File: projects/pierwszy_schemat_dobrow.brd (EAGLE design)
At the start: 100 x 80 mm, 36 parts, among them IC1 74HC595N, IC2 7805T, IC3 LD117AV

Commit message: Done power section
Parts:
- moved IC2 178.9 mm to (90.1, 63.9), flipped to the bottom, turned to 90 degrees
- moved C2 142.0 mm to (85.2, 74.5), turned to 90 degrees
- moved IC3 123.7 mm to (70.0, 64.0), turned to 90 degrees
- moved C1 119.9 mm to (74.4, 74.3), turned to 90 degrees
- moved U$1 14.3 mm to (51.0, 38.9)
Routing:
- net GND: track 0.00 -> 34.0 mm, vias 0 -> 1
- net VCC_5V: track 0.00 -> 13.8 mm
- net VIN_9V: track 0.00 -> 12.8 mm, vias 0 -> 1

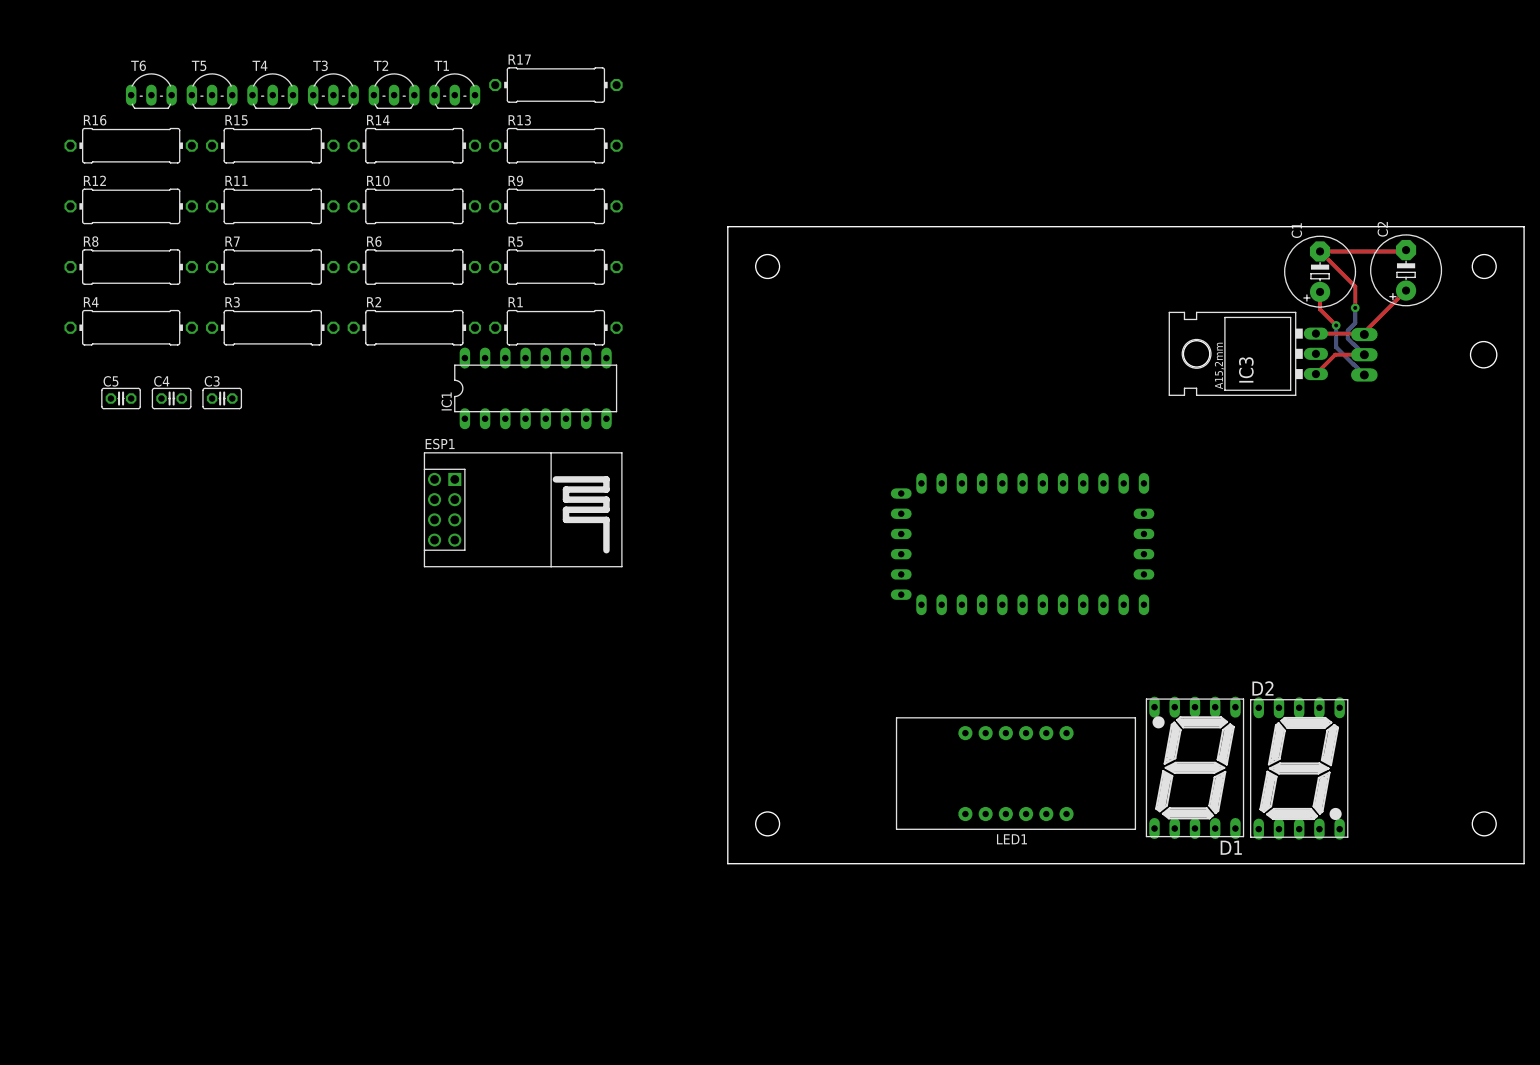
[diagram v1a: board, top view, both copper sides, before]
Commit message: Added ESP-01 module
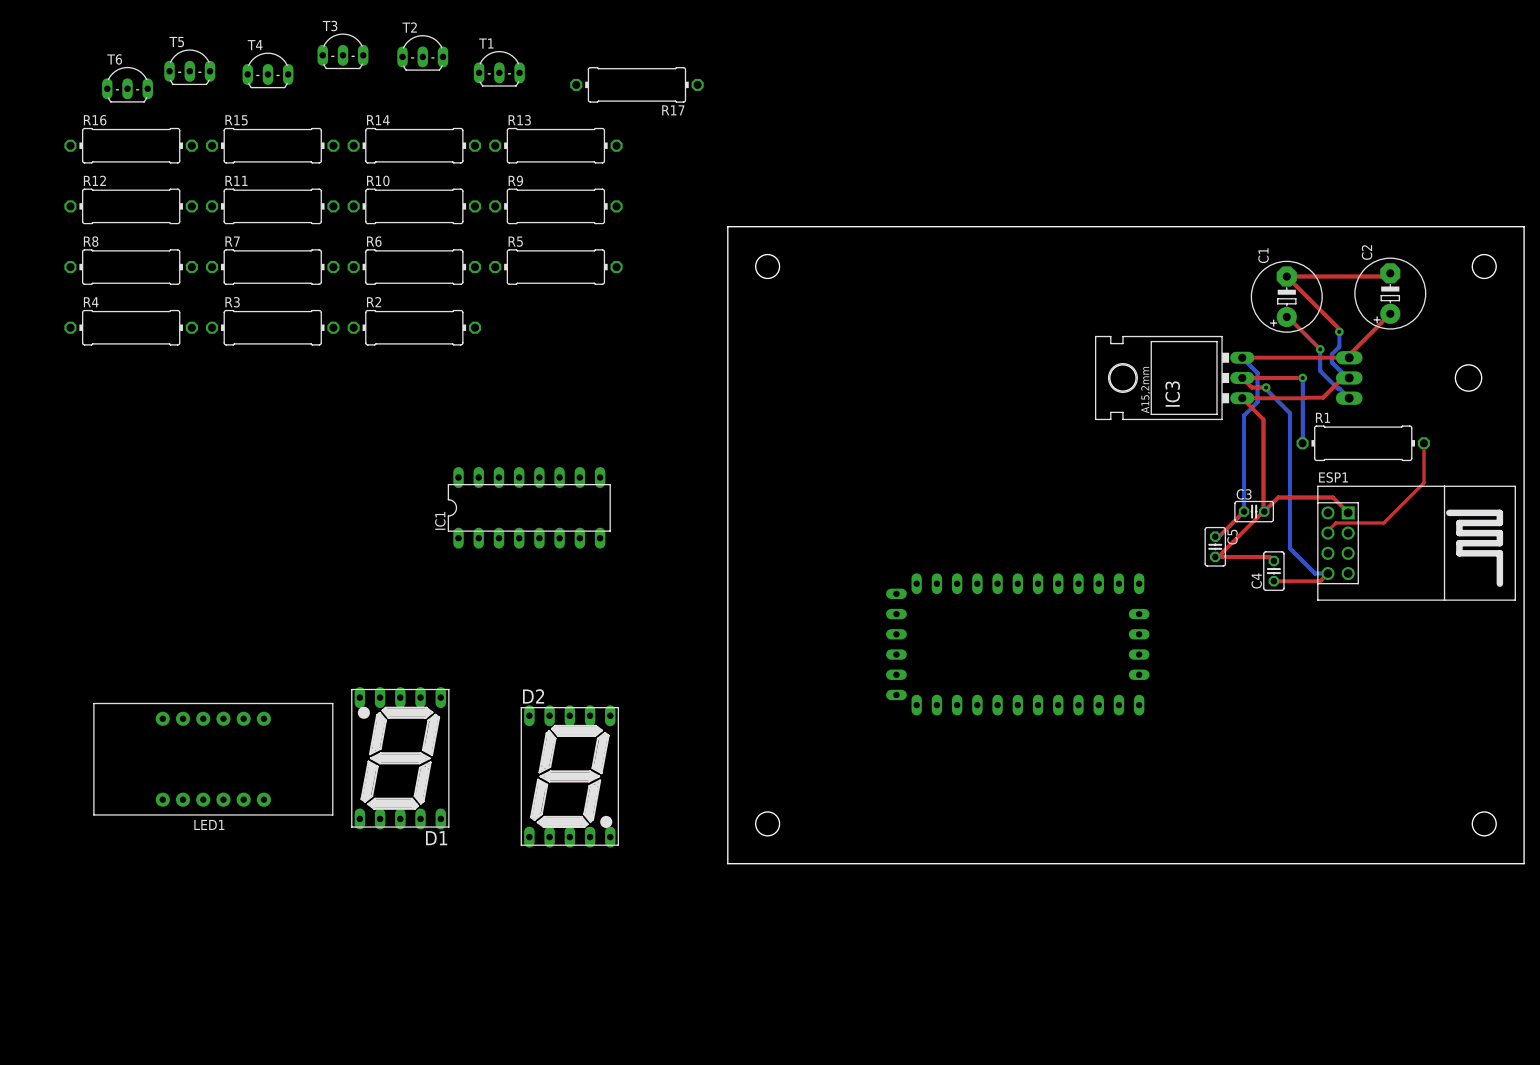
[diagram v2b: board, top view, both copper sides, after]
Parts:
- moved C4 140.1 mm to (68.6, 36.8), turned to 90 degrees
- moved C5 138.7 mm to (61.2, 39.8), turned to 270 degrees
- moved C3 130.4 mm to (66.1, 44.2)
- moved ESP1 112.3 mm to (74.1, 40.2)
- moved R1 102.4 mm to (79.8, 52.8)
- moved LED1 100.8 mm to (-64.6, 13.1)
- moved D1 99.8 mm to (-41.1, 13.2)
- moved D2 91.6 mm to (-19.8, 11.0)
- moved IC1 15.0 mm to (-24.9, 44.7)
- moved U$1 12.6 mm to (50.4, 26.3)
- moved R17 10.2 mm to (-11.4, 97.8), turned to 180 degrees
- moved IC3 9.73 mm to (60.8, 61.0)
- moved T1 6.26 mm to (-28.7, 100.6)
- moved T2 6.00 mm to (-38.3, 102.6)
- moved C1 5.23 mm to (70.2, 71.2)
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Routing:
- net GND: track 34.0 -> 88.1 mm
- net VCC_3V3: track 0.00 -> 54.0 mm, vias 0 -> 2
- net VCC_5V: track 13.8 -> 46.8 mm
- net N$10: track 0.00 -> 19.8 mm
- net VIN_9V: track 12.8 -> 13.7 mm

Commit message: Connected display module
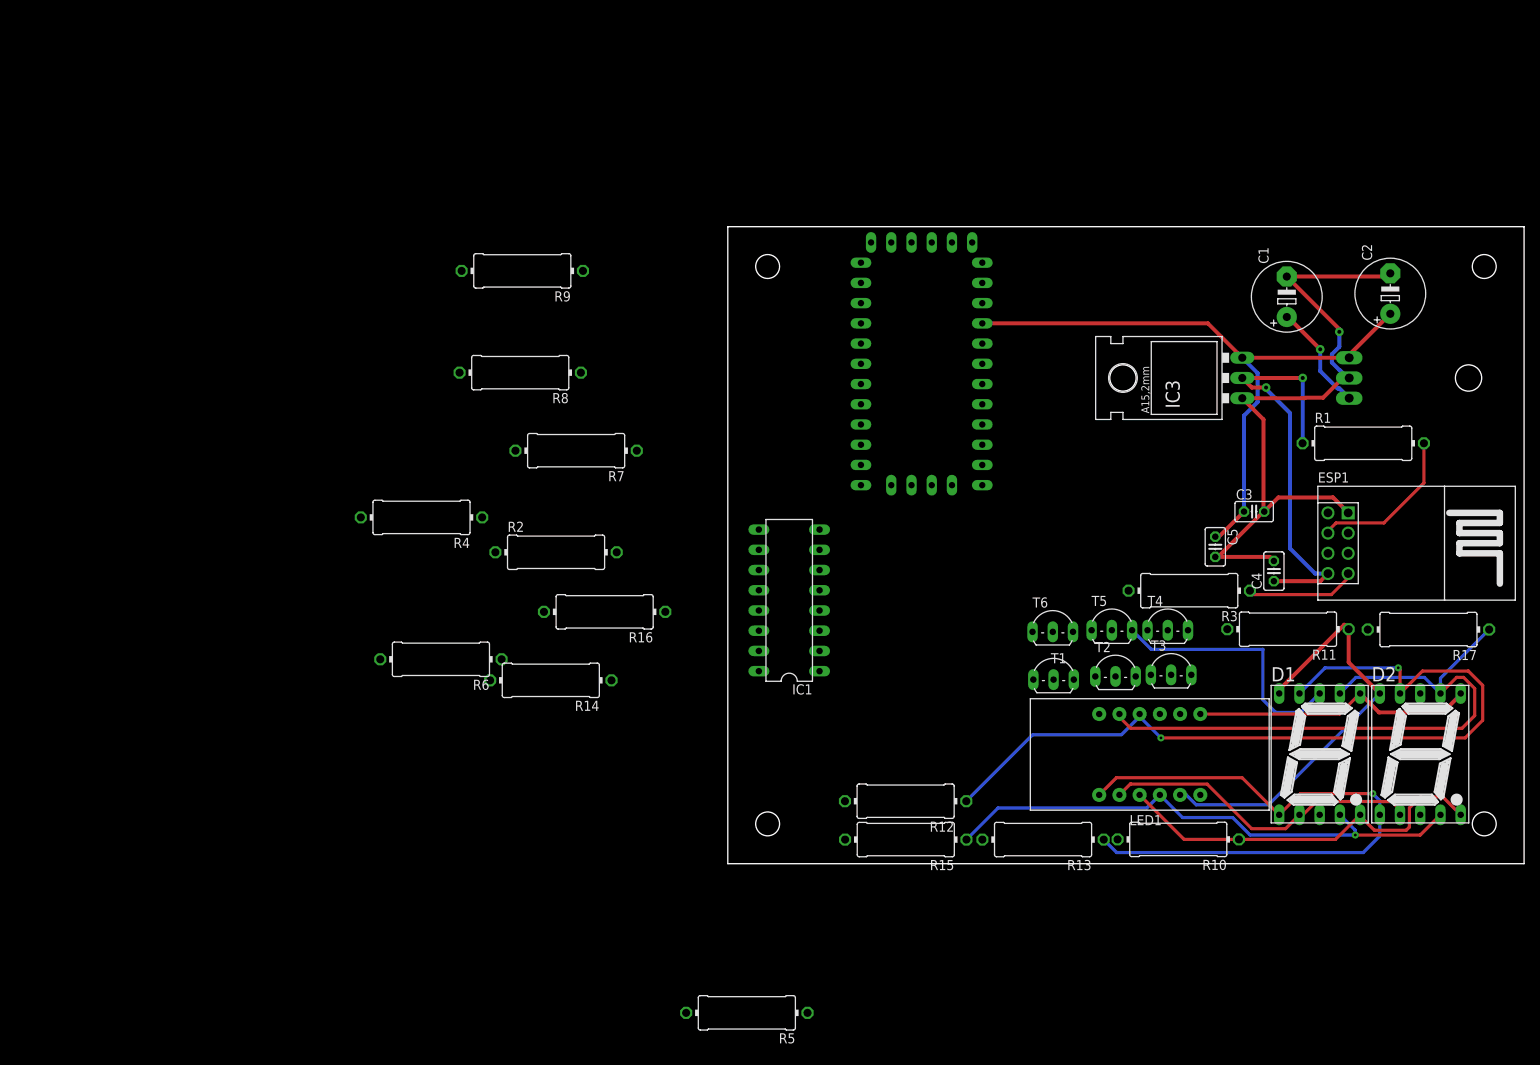
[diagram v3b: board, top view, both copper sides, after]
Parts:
- moved R11 138.1 mm to (70.3, 29.4), turned to 180 degrees
- moved T5 135.4 mm to (48.2, 30.6)
- moved T6 134.7 mm to (40.8, 30.4)
- moved T4 132.8 mm to (55.2, 30.6)
- moved T3 129.9 mm to (55.7, 25.0)
- moved R10 124.6 mm to (56.6, 3.05), turned to 180 degrees
- moved R12 122.6 mm to (22.3, 7.85), turned to 180 degrees
- moved R17 120.7 mm to (88.0, 29.4)
- moved R3 119.7 mm to (58.0, 34.3), turned to 180 degrees
- moved R15 118.0 mm to (22.4, 3.03), turned to 180 degrees
- moved LED1 117.6 mm to (53.0, 13.7)
- moved T2 116.7 mm to (48.7, 24.8)
- moved D1 115.5 mm to (74.3, 13.8), turned to 0 degrees
- moved D2 106.8 mm to (87.0, 13.8)
- moved R13 106.5 mm to (39.6, 3.03), turned to 180 degrees
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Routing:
- net SEG_F: track 0.00 -> 105.8 mm, vias 0 -> 2
- net SEG_A: track 0.00 -> 80.2 mm
- net SEG_E: track 0.00 -> 80.2 mm, vias 0 -> 1
- net SEG_C: track 0.00 -> 68.3 mm, vias 0 -> 1
- net SEG_G: track 0.00 -> 53.9 mm
- net SEG_H: track 0.00 -> 48.9 mm
- net SEG_D: track 0.00 -> 40.7 mm
- net SEG_B: track 0.00 -> 35.8 mm
- net VCC_5V: track 46.8 -> 81.3 mm
- net N$29: track 0.00 -> 32.5 mm
- net TX_ARDUINO: track 0.00 -> 13.9 mm

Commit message: Update pierwszy_schemat_dobrow.brd
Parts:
- moved R5 67.8 mm to (22.2, 46.1), turned to 0 degrees
- moved R4 63.1 mm to (22.3, 26.3), turned to 0 degrees
- moved R2 61.1 mm to (39.4, 35.9)
- moved R9 58.7 mm to (22.2, 40.6)
- moved R6 58.4 mm to (22.2, 21.5), turned to 0 degrees
- moved R8 54.8 mm to (22.3, 35.9), turned to 0 degrees
- moved R7 46.2 mm to (22.2, 31.1), flipped to the bottom
- moved R14 45.9 mm to (22.4, 12.0)
- moved R16 40.6 mm to (22.3, 16.8)
- moved U$1 21.1 mm to (4.81, 59.3), turned to 270 degrees
- moved IC1 7.62 mm to (7.11, 25.5)
- moved C4 3.24 mm to (66.0, 38.8), turned to 180 degrees
- moved R3 2.00 mm to (56.8, 35.9)
- moved C5 1.65 mm to (61.6, 41.4)
- moved R10 0.63 mm to (56.8, 2.45)
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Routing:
- net N$7: track 0.00 -> 35.2 mm
- net N$28: track 0.00 -> 22.9 mm, vias 0 -> 1
- net TX_ARDUINO: track 13.9 -> 33.1 mm
- net VCC_5V: track 81.3 -> 89.8 mm
- net N$27: track 0.00 -> 5.75 mm
- net N$8: track 0.00 -> 5.73 mm
- net N$26: track 0.00 -> 5.39 mm
- net GND: track 88.1 -> 83.9 mm
- net VCC_3V3: track 54.0 -> 55.8 mm
- net SEG_D: track 40.7 -> 42.1 mm
- net SEG_H: track 48.9 -> 50.0 mm
- net SEG_F: track 105.8 -> 106.6 mm
- net SEG_B: track 35.8 -> 36.4 mm
- net SEG_G: track 53.9 -> 54.5 mm

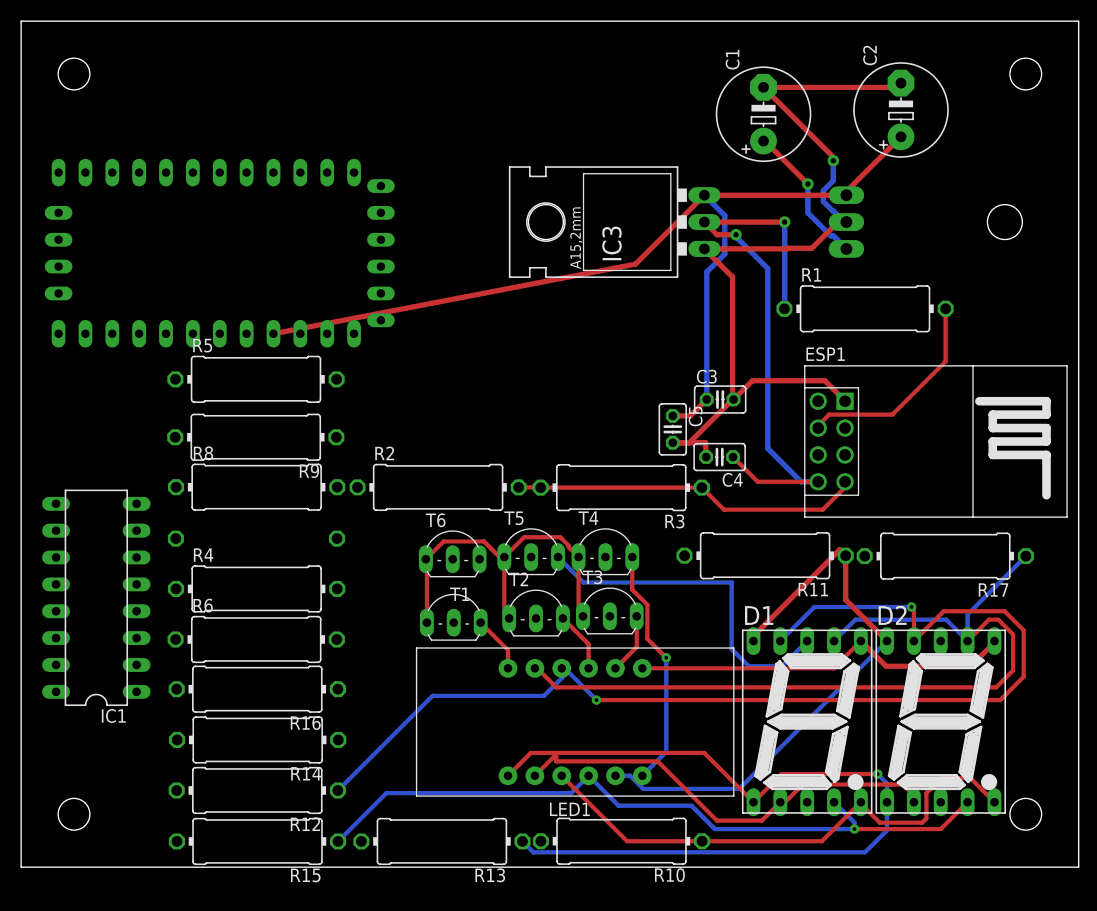
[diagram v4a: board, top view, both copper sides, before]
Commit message: Completed first revision of pcb design
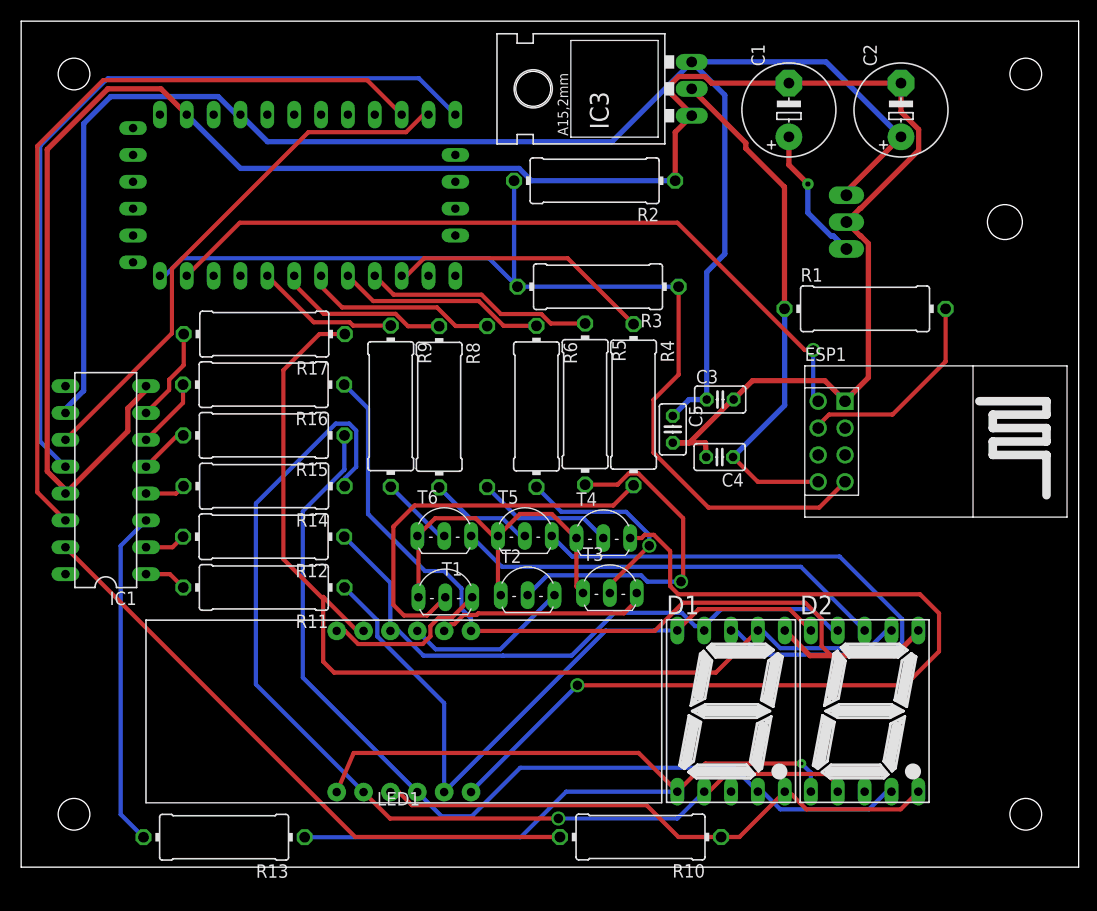
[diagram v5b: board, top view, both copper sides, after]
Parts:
- moved R17 67.7 mm to (23.0, 50.4)
- moved R11 47.5 mm to (22.9, 26.4)
- moved R4 39.7 mm to (57.9, 43.7), turned to 270 degrees
- moved R15 38.4 mm to (22.9, 40.8)
- moved U$1 35.1 mm to (39.8, 62.3), turned to 90 degrees
- moved R6 34.5 mm to (48.7, 43.6), turned to 270 degrees
- moved R2 32.6 mm to (54.2, 64.9), turned to 180 degrees
- moved R5 31.2 mm to (53.3, 43.8), turned to 270 degrees
- moved R16 28.8 mm to (22.9, 45.6)
- moved R7 25.1 mm to (44.1, 43.5), turned to 270 degrees
- moved R12 24.0 mm to (22.9, 31.2)
- moved R14 24.0 mm to (23.0, 36.0)
- moved R13 20.6 mm to (19.2, 2.83)
- moved R3 19.1 mm to (54.5, 54.9)
- moved R8 18.9 mm to (39.5, 43.5), turned to 270 degrees
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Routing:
- net GND: track 83.9 -> 204.6 mm, vias 1 -> 0
- net DATA_PIN: track 0.00 -> 74.9 mm
- net LATCH_PIN: track 0.00 -> 74.7 mm
- net RX_ARDUINO: track 0.00 -> 71.3 mm, vias 0 -> 1
- net VCC_5V: track 89.8 -> 160.3 mm
- net TX_ARDUINO: track 33.1 -> 99.4 mm
- net N$28: track 22.9 -> 87.7 mm
- net N$12: track 0.00 -> 58.1 mm
- net SEG_D: track 42.1 -> 98.8 mm, vias 0 -> 1
- net CLOCK_PIN: track 0.00 -> 50.7 mm
- net SEG_F: track 106.6 -> 58.1 mm, vias 2 -> 0
- net SEG_B: track 36.4 -> 82.7 mm
- net N$30: track 0.00 -> 40.9 mm
- net N$1: track 0.00 -> 37.8 mm
- net N$2: track 0.00 -> 33.1 mm, vias 0 -> 1
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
